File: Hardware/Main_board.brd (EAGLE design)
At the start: 100 x 80 mm, 19 parts, among them IC1 MEGA8-AI, IC2 LP2950CZ-3.0

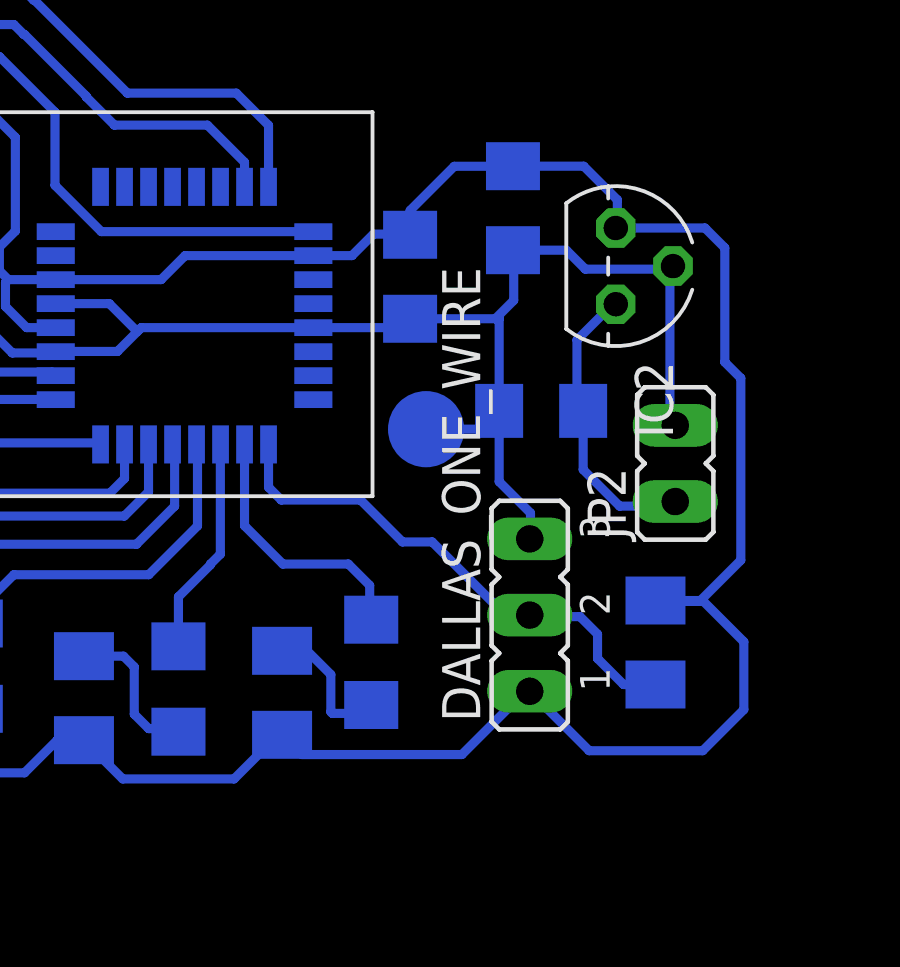
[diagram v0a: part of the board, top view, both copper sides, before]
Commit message: added battery voltage sensing HW
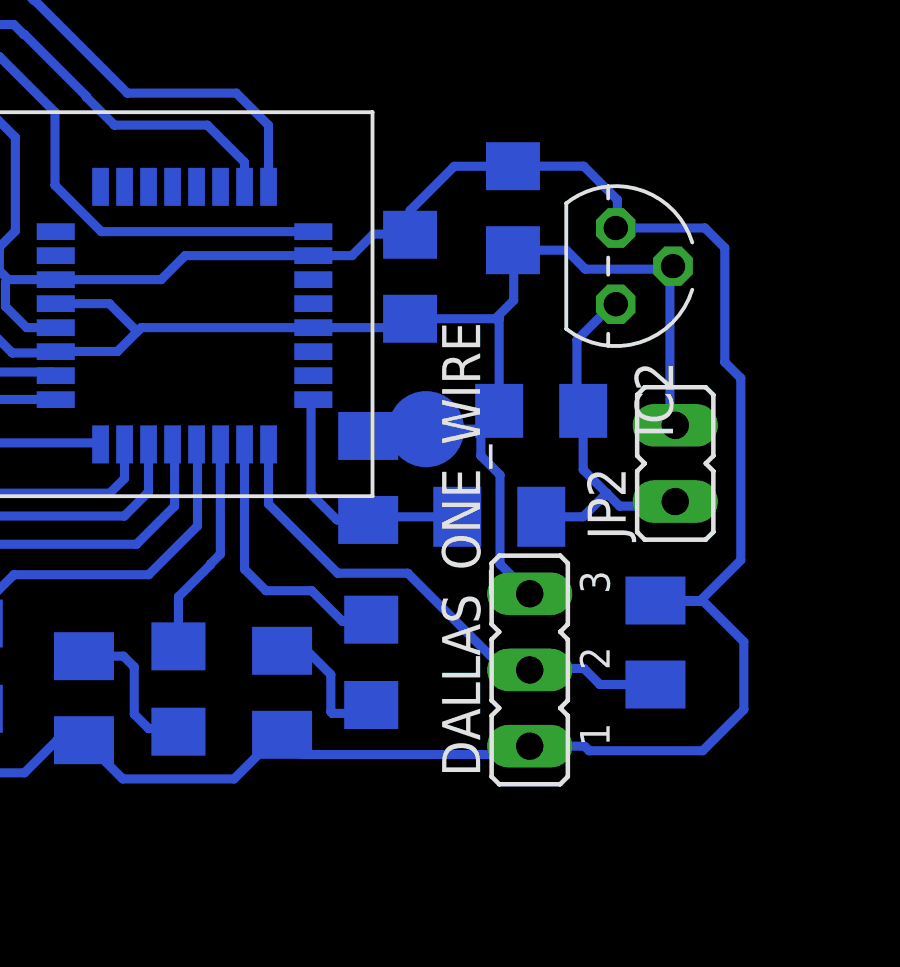
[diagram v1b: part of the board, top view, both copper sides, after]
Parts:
- added R6: 50k, resistor:M1206
- added R7: 100k, resistor:M1206
- moved DALLAS_ONE_WIRE 1.83 mm to (70.8, 31.0)
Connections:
- new net BATT: IC1.24, R6.1, R7.1
- net GND: now also R7.2
- net V+: now also R6.2
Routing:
- net BATT: track 0.00 -> 8.45 mm
- net GND: track 52.5 -> 56.0 mm
- net V+: track 9.83 -> 12.3 mm
- net +3V3: track 103.1 -> 101.6 mm
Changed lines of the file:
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@@
 <element name="C3" library="rcl" package="C1206" value="100n" x="66.802" y="44.0944" rot="MR270"/>
 <element name="C4" library="rcl" package="C1206" value="100n" x="51.6636" y="48.3362" rot="MR270"/>
-<element name="DALLAS_ONE_WIRE" library="jumper" package="JP2" value="" x="70.7898" y="32.8168" rot="R90"/>
+<element name="DALLAS_ONE_WIRE" library="jumper" package="JP2" value="" x="70.7898" y="30.988" rot="R90"/>
 <element name="R1" library="rcl" package="M1206" value="4k7" x="74.9808" y="31.9024" rot="MR90"/>
 <element name="LED1" library="led" package="1206" value="" x="65.5066" y="31.242" rot="MR90"/>
@@
 <attribute name="TP_SIGNAL_NAME" value="" x="67.3354" y="39.0144" size="1.778" layer="28" rot="MR0" display="off"/>
 </element>
+<element name="R6" library="resistor" package="M1206" value="50k" x="69.7738" y="36.0934" rot="MR180"/>
+<element name="R7" library="resistor" package="M1206" value="100k" x="65.405" y="37.3888" rot="MR90"/>
 </elements>
 <signals>
@@
 <wire x1="72.5708" y1="39.624" x2="72.3646" y2="39.8302" width="0.3048" layer="16"/>
 <wire x1="72.5708" y1="37.6652" x2="72.5708" y2="39.624" width="0.3048" layer="16"/>
-<wire x1="72.5708" y1="37.6652" x2="73.787" y2="36.449" width="0.3048" layer="16"/>
+<wire x1="72.5708" y1="37.6652" x2="73.3552" y2="36.8808" width="0.3048" layer="16"/>
+<wire x1="73.3552" y1="36.8808" x2="73.787" y2="36.449" width="0.3048" layer="16"/>
 <wire x1="73.787" y1="36.449" x2="75.4888" y2="36.449" width="0.3048" layer="16"/>
 <wire x1="75.4888" y1="36.449" x2="75.6412" y2="36.6014" width="0.3048" layer="16"/>
+<contactref element="R6" pad="2"/>
+<wire x1="71.1738" y1="36.0934" x2="72.5678" y2="36.0934" width="0.3048" layer="16"/>
+<wire x1="72.5678" y1="36.0934" x2="73.3552" y2="36.8808" width="0.3048" layer="16"/>
 </signal>
 <signal name="+3V3">
@@
 <wire x1="76.5556" y1="28.2956" x2="77.9272" y2="29.6672" width="0.3048" layer="16"/>
 <wire x1="72.771" y1="28.2956" x2="76.5556" y2="28.2956" width="0.3048" layer="16"/>
-<wire x1="70.7898" y1="30.2768" x2="72.771" y2="28.2956" width="0.3048" layer="16"/>
 <wire x1="58.5024" y1="43.999" x2="54.991" y2="43.999" width="0.3048" layer="16"/>
 <wire x1="63.5762" y1="44.799" x2="59.3024" y2="44.799" width="0.3048" layer="16"/>
@@
 <wire x1="48.514" y1="46.7106" x2="49.3494" y2="46.7106" width="0.3048" layer="16"/>
 <wire x1="49.3494" y1="46.7106" x2="49.45" y2="46.61" width="0.3048" layer="16"/>
-<wire x1="70.6374" y1="30.2768" x2="70.7898" y2="30.2768" width="0.3048" layer="16"/>
-<wire x1="68.5292" y1="28.1686" x2="70.6374" y2="30.2768" width="0.3048" layer="16"/>
-<wire x1="63.1922" y1="28.1686" x2="68.5292" y2="28.1686" width="0.3048" layer="16"/>
+<wire x1="63.1922" y1="28.1686" x2="70.5104" y2="28.1686" width="0.3048" layer="16"/>
 <wire x1="62.5348" y1="28.826" x2="63.1922" y2="28.1686" width="0.3048" layer="16"/>
 <wire x1="62.4048" y1="28.826" x2="62.5348" y2="28.826" width="0.3048" layer="16"/>
@@
 <wire x1="45.3644" y1="30.096" x2="48.7426" y2="30.096" width="0.3048" layer="16"/>
 <wire x1="45.0088" y1="30.4516" x2="45.3644" y2="30.096" width="0.3048" layer="16"/>
+<wire x1="70.5104" y1="28.1686" x2="70.7898" y2="28.448" width="0.3048" layer="16"/>
+<wire x1="70.7898" y1="28.448" x2="72.6186" y2="28.448" width="0.3048" layer="16"/>
+<wire x1="72.6186" y1="28.448" x2="72.771" y2="28.2956" width="0.3048" layer="16"/>
 </signal>
 <signal name="GND">
@@
 <wire x1="69.6438" y1="42.6944" x2="69.7708" y2="42.6944" width="0.3048" layer="16"/>
 <wire x1="69.7708" y1="42.6944" x2="69.7708" y2="39.624" width="0.3048" layer="16"/>
-<wire x1="69.7708" y1="39.624" x2="69.7708" y2="37.2648" width="0.3048" layer="16"/>
-<wire x1="69.7708" y1="37.2648" x2="70.8152" y2="36.2204" width="0.3048" layer="16"/>
-<wire x1="70.8152" y1="36.2204" x2="70.8152" y2="35.3822" width="0.3048" layer="16"/>
-<wire x1="70.8152" y1="35.3822" x2="70.7898" y2="35.3568" width="0.3048" layer="16"/>
 <wire x1="57.8422" y1="42.399" x2="63.5762" y2="42.399" width="0.3048" layer="16"/>
 <wire x1="57.0484" y1="41.6052" x2="57.7088" y2="42.2656" width="0.3048" layer="16"/>
@@
 <wire x1="67.3354" y1="39.0144" x2="69.1612" y2="39.0144" width="0.3048" layer="16"/>
 <wire x1="69.1612" y1="39.0144" x2="69.7708" y2="39.624" width="0.3048" layer="16"/>
+<contactref element="R7" pad="2"/>
+<wire x1="65.405" y1="38.7888" x2="67.1098" y2="38.7888" width="0.3048" layer="16"/>
+<wire x1="67.1098" y1="38.7888" x2="67.3354" y2="39.0144" width="0.3048" layer="16"/>
+<wire x1="69.1612" y1="39.0144" x2="69.1612" y2="38.1284" width="0.3048" layer="16"/>
+<wire x1="69.1612" y1="38.1284" x2="69.7992" y2="37.4904" width="0.3048" layer="16"/>
+<wire x1="69.7992" y1="37.4904" x2="69.7992" y2="34.5186" width="0.3048" layer="16"/>
+<wire x1="69.7992" y1="34.5186" x2="70.7898" y2="33.528" width="0.3048" layer="16"/>
 </signal>
 <signal name="RXTX">
@@
 <contactref element="R1" pad="1"/>
 <contactref element="IC1" pad="25"/>
-<wire x1="73.917" y1="30.5024" x2="74.9808" y2="30.5024" width="0.3048" layer="16"/>
-<wire x1="73.0504" y1="31.369" x2="73.917" y2="30.5024" width="0.3048" layer="16"/>
-<wire x1="73.0504" y1="32.1818" x2="73.0504" y2="31.369" width="0.3048" layer="16"/>
-<wire x1="72.4662" y1="32.766" x2="73.0504" y2="32.1818" width="0.3048" layer="16"/>
-<wire x1="70.9676" y1="32.766" x2="72.4662" y2="32.766" width="0.3048" layer="16"/>
-<wire x1="70.7898" y1="32.8168" x2="70.9676" y2="32.766" width="0.3048" layer="16"/>
-<wire x1="69.8754" y1="32.9184" x2="70.7898" y2="32.8168" width="0.3048" layer="16"/>
-<wire x1="67.5386" y1="35.2552" x2="69.8754" y2="32.9184" width="0.3048" layer="16"/>
-<wire x1="66.548" y1="35.2552" x2="67.5386" y2="35.2552" width="0.3048" layer="16"/>
-<wire x1="62.0836" y1="37.078" x2="62.0836" y2="38.5064" width="0.3048" layer="16"/>
-<wire x1="62.5094" y1="36.6522" x2="62.0836" y2="37.078" width="0.3048" layer="16"/>
-<wire x1="62.5094" y1="36.6522" x2="65.151" y2="36.6522" width="0.3048" layer="16"/>
-<wire x1="65.151" y1="36.6522" x2="66.548" y2="35.2552" width="0.3048" layer="16"/>
+<wire x1="74.9808" y1="30.5024" x2="73.1296" y2="30.5024" width="0.3048" layer="16"/>
+<wire x1="73.1296" y1="30.5024" x2="72.5932" y2="31.0388" width="0.3048" layer="16"/>
+<wire x1="72.5932" y1="31.0388" x2="70.8406" y2="31.0388" width="0.3048" layer="16"/>
+<wire x1="70.8406" y1="31.0388" x2="70.7898" y2="30.988" width="0.3048" layer="16"/>
+<wire x1="70.7898" y1="30.988" x2="69.9516" y2="30.988" width="0.3048" layer="16"/>
+<wire x1="69.9516" y1="30.988" x2="66.7258" y2="34.2138" width="0.3048" layer="16"/>
+<wire x1="66.7258" y1="34.2138" x2="64.389" y2="34.2138" width="0.3048" layer="16"/>
+<wire x1="64.389" y1="34.2138" x2="62.0836" y2="36.5192" width="0.3048" layer="16"/>
+<wire x1="62.0836" y1="36.5192" x2="62.0836" y2="38.5064" width="0.3048" layer="16"/>
 </signal>
 <signal name="N$1">
@@
 <contactref element="LED1" pad="C"/>
 <contactref element="IC1" pad="26"/>
-<wire x1="61.2836" y1="35.7952" x2="61.2836" y2="38.5064" width="0.3048" layer="16"/>
-<wire x1="62.5602" y1="34.5186" x2="61.2836" y2="35.7952" width="0.3048" layer="16"/>
-<wire x1="64.7446" y1="34.5186" x2="62.5602" y2="34.5186" width="0.3048" layer="16"/>
-<wire x1="65.4558" y1="33.8074" x2="64.7446" y2="34.5186" width="0.3048" layer="16"/>
-<wire x1="65.4558" y1="32.7148" x2="65.4558" y2="33.8074" width="0.3048" layer="16"/>
+<wire x1="61.2836" y1="34.3474" x2="61.2836" y2="38.5064" width="0.3048" layer="16"/>
 <wire x1="65.5066" y1="32.664" x2="65.4558" y2="32.7148" width="0.3048" layer="16"/>
+<wire x1="61.2836" y1="34.3474" x2="62.0014" y2="33.6296" width="0.3048" layer="16"/>
+<wire x1="62.0014" y1="33.6296" x2="63.5254" y2="33.6296" width="0.3048" layer="16"/>
+<wire x1="63.5254" y1="33.6296" x2="64.5414" y2="32.6136" width="0.3048" layer="16"/>
+<wire x1="64.5414" y1="32.6136" x2="65.4562" y2="32.6136" width="0.3048" layer="16"/>
+<wire x1="65.4562" y1="32.6136" x2="65.5066" y2="32.664" width="0.3048" layer="16"/>
 </signal>
 <signal name="LED2">
@@
 <wire x1="44.8818" y1="36.068" x2="44.9326" y2="36.1188" width="0.3048" layer="16"/>
 </signal>
+<signal name="BATT">
+<contactref element="R6" pad="1"/>
+<contactref element="R7" pad="1"/>
+<contactref element="IC1" pad="24"/>
+<wire x1="65.405" y1="35.9888" x2="65.5096" y2="36.0934" width="0.3048" layer="16"/>
+<wire x1="65.5096" y1="36.0934" x2="68.3738" y2="36.0934" width="0.3048" layer="16"/>
+<wire x1="65.405" y1="35.9888" x2="64.3666" y2="35.9888" width="0.3048" layer="16"/>
+<wire x1="64.3666" y1="35.9888" x2="63.5" y2="36.8554" width="0.3048" layer="16"/>
+<wire x1="63.5" y1="36.8554" x2="63.5" y2="39.9228" width="0.3048" layer="16"/>
+<wire x1="63.5" y1="39.9228" x2="63.5762" y2="39.999" width="0.3048" layer="16"/>
+</signal>
 </signals>
